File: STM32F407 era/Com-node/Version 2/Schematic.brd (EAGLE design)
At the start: 127 x 165.1 mm, 92 parts, among them IC2 lm2575, IC5 REG1117, Q2 12MHz, Q3 12MHz, U1 MAX13052ESA+, U2 SMS05, U3 MAX232AEWE+, X1 SDBMF, X5 679105700

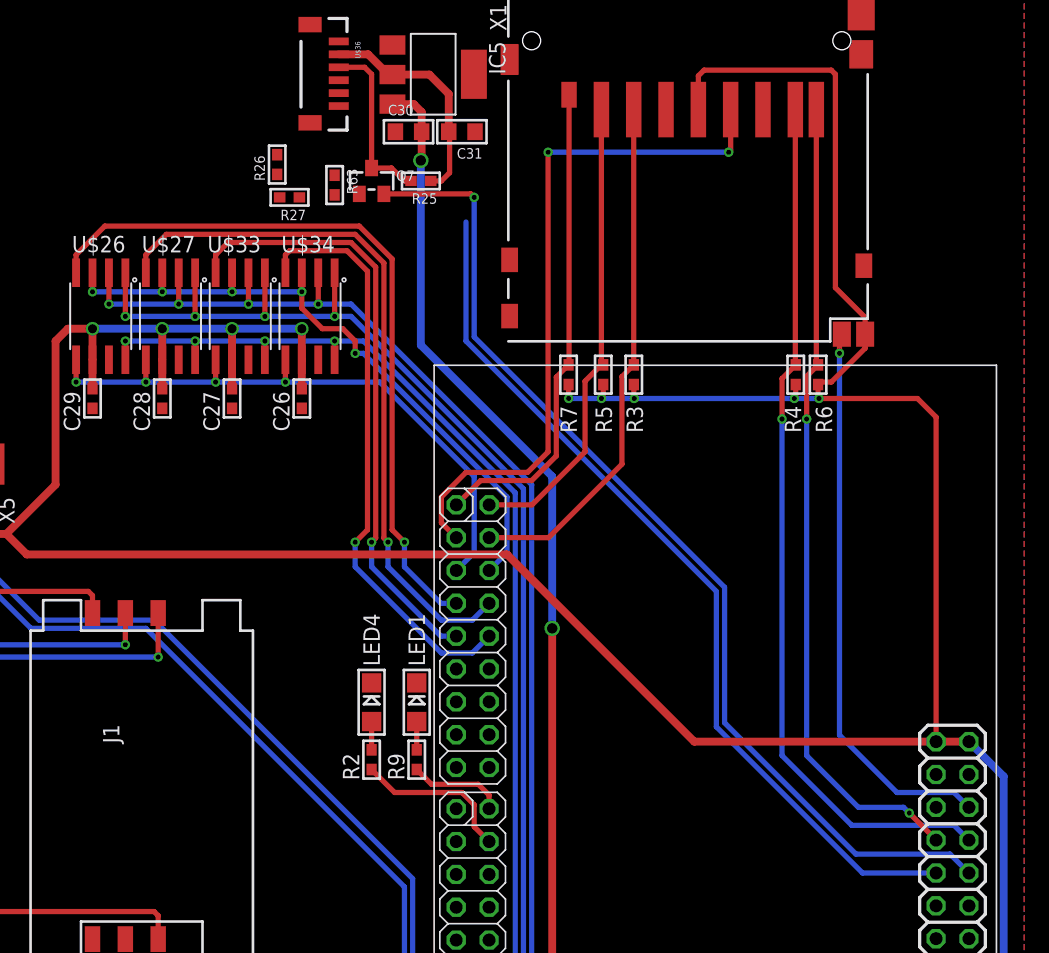
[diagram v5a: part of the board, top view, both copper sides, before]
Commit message: continued work on H-bridge
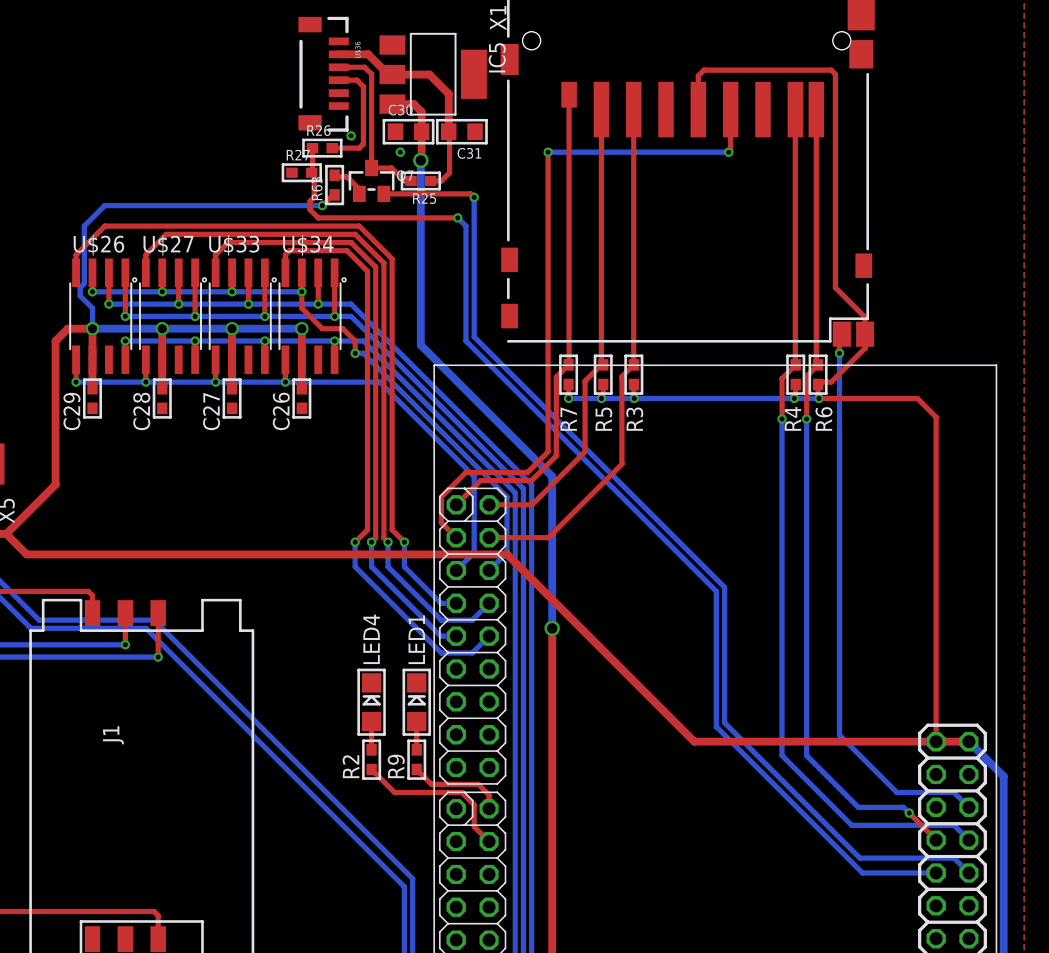
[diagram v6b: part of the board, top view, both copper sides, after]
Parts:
- moved R26 3.72 mm to (64.8, 140.3), turned to 0 degrees
- moved R27 2.13 mm to (63.2, 138.4), turned to 0 degrees
- turned R63 to 90 degrees
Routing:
- net 3.3V: track 573.3 -> 602.1 mm, vias 15 -> 16
- net GPS_RX: track 68.8 -> 86.0 mm, vias 0 -> 1
- net RXD1: track 0.00 -> 9.10 mm
- net N$58: track 0.00 -> 2.72 mm
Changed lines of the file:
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@@
 <element name="Q7" library="microbuilder" package="SOT23-WIDE" value="" x="68.58" y="137.795"/>
 <element name="R25" library="microbuilder" package="_0603" value="500" x="72.39" y="137.795" rot="R180"/>
-<element name="R63" library="microbuilder" package="_0603" value="500" x="65.7225" y="137.4775" rot="R270"/>
-<element name="R26" library="microbuilder" package="_0603" value="499" x="61.2775" y="139.065" rot="R90"/>
-<element name="R27" library="microbuilder" package="_0603" value="976" x="62.23" y="136.525" rot="R180"/>
+<element name="R63" library="microbuilder" package="_0603" value="500" x="65.7225" y="137.4775" rot="R90"/>
+<element name="R26" library="microbuilder" package="_0603" value="499" x="64.77" y="140.335"/>
+<element name="R27" library="microbuilder" package="_0603" value="976" x="63.1825" y="138.43"/>
 </elements>
 <signals>
@@
 <contactref element="C31" pad="1"/>
 <contactref element="R27" pad="1"/>
-<wire x1="70.4215" y1="141.605" x2="66.04" y2="144.59" width="0" layer="19" extent="1-1"/>
+<via x="70.8025" y="140.0175" extent="1-16" drill="0.381"/>
+<via x="66.9925" y="141.2875" extent="1-16" drill="0.381"/>
 </signal>
 <signal name="3.3V">
@@
 <wire x1="112.2045" y1="24.5745" x2="113.03" y2="24.5745" width="0.6096" layer="1"/>
 <contactref element="R63" pad="1"/>
-<wire x1="63.1825" y1="126.365" x2="65.7225" y2="138.2395" width="0" layer="19" extent="1-1"/>
+<wire x1="65.7225" y1="136.7155" x2="65.5955" y2="136.7155" width="0.4064" layer="1"/>
+<wire x1="65.5955" y1="136.7155" x2="64.77" y2="135.89" width="0.4064" layer="1"/>
+<via x="64.77" y="135.89" extent="1-16" drill="0.381"/>
+<wire x1="64.77" y1="135.89" x2="47.9425" y2="135.89" width="0.4064" layer="16"/>
+<wire x1="47.9425" y1="135.89" x2="46.355" y2="134.3025" width="0.4064" layer="16"/>
+<wire x1="46.355" y1="134.3025" x2="46.355" y2="129.8575" width="0.4064" layer="16"/>
+<wire x1="46.355" y1="129.8575" x2="46.0375" y2="129.54" width="0.4064" layer="16"/>
+<wire x1="46.0375" y1="129.54" x2="46.0375" y2="128.905" width="0.4064" layer="16"/>
+<wire x1="46.0375" y1="128.905" x2="46.99" y2="127.9525" width="0.4064" layer="16"/>
+<wire x1="46.99" y1="127.9525" x2="46.99" y2="126.365" width="0.4064" layer="16"/>
 </signal>
 <signal name="N$1">
@@
 <contactref element="U$36" pad="4"/>
 <contactref element="R26" pad="2"/>
-<wire x1="61.2775" y1="139.827" x2="66.04" y2="145.59" width="0" layer="19" extent="1-1"/>
+<wire x1="66.04" y1="145.59" x2="67.4525" y2="145.59" width="0.4064" layer="1"/>
+<wire x1="67.4525" y1="145.59" x2="67.945" y2="145.0975" width="0.4064" layer="1"/>
+<wire x1="67.945" y1="145.0975" x2="67.945" y2="140.6525" width="0.4064" layer="1"/>
+<wire x1="67.945" y1="140.6525" x2="67.6275" y2="140.335" width="0.4064" layer="1"/>
+<wire x1="67.6275" y1="140.335" x2="65.532" y2="140.335" width="0.4064" layer="1"/>
 </signal>
 <signal name="GPS_RX">
@@
 <wire x1="95.25" y1="95.5675" x2="95.25" y2="106.045" width="0.4064" layer="16"/>
 <wire x1="95.25" y1="106.045" x2="75.8825" y2="125.4125" width="0.4064" layer="16"/>
-<wire x1="75.8825" y1="125.4125" x2="75.8825" y2="134.62" width="0.4064" layer="16"/>
-<wire x1="61.468" y1="136.525" x2="61.2775" y2="138.303" width="0" layer="19" extent="1-1"/>
-<wire x1="75.8825" y1="134.62" x2="61.468" y2="136.525" width="0" layer="19" extent="1-16"/>
+<wire x1="75.8825" y1="125.4125" x2="75.8825" y2="134.3025" width="0.4064" layer="16"/>
+<wire x1="64.008" y1="140.335" x2="64.008" y2="138.4935" width="0.4064" layer="1"/>
+<wire x1="64.008" y1="138.4935" x2="63.9445" y2="138.43" width="0.4064" layer="1"/>
+<wire x1="63.8175" y1="135.5725" x2="64.4525" y2="134.9375" width="0.4064" layer="1"/>
+<wire x1="64.4525" y1="134.9375" x2="75.2475" y2="134.9375" width="0.4064" layer="1"/>
+<via x="75.2475" y="134.9375" extent="1-16" drill="0.381"/>
+<wire x1="75.2475" y1="134.9375" x2="75.8825" y2="134.3025" width="0.4064" layer="16"/>
+<wire x1="63.8175" y1="135.5725" x2="63.8175" y2="136.2075" width="0.4064" layer="1"/>
+<wire x1="63.8175" y1="136.2075" x2="64.135" y2="136.525" width="0.4064" layer="1"/>
+<wire x1="64.135" y1="136.525" x2="64.135" y2="138.2395" width="0.4064" layer="1"/>
+<wire x1="64.135" y1="138.2395" x2="63.9445" y2="138.43" width="0.4064" layer="1"/>
 </signal>
 <signal name="GPS_TX">
 <contactref element="U$1" pad="P$35"/>
 <contactref element="Q7" pad="2"/>
-<wire x1="114.78745" y1="84.26215" x2="113.3246" y2="85.725" width="0.4064" layer="16"/>
-<wire x1="113.3246" y1="85.725" x2="106.045" y2="85.725" width="0.4064" layer="16"/>
-<wire x1="106.045" y1="85.725" x2="95.885" y2="95.885" width="0.4064" layer="16"/>
+<wire x1="114.78745" y1="84.26215" x2="113.6421" y2="85.4075" width="0.4064" layer="16"/>
+<wire x1="113.6421" y1="85.4075" x2="106.3625" y2="85.4075" width="0.4064" layer="16"/>
+<wire x1="106.3625" y1="85.4075" x2="95.885" y2="95.885" width="0.4064" layer="16"/>
 <wire x1="95.885" y1="95.885" x2="95.885" y2="106.3625" width="0.4064" layer="16"/>
 <wire x1="95.885" y1="106.3625" x2="76.5175" y2="125.73" width="0.4064" layer="16"/>
@@
 <contactref element="Q7" pad="1"/>
 <contactref element="R63" pad="2"/>
-<wire x1="65.7225" y1="136.7155" x2="67.63" y2="136.795" width="0" layer="19" extent="1-1"/>
+<wire x1="67.63" y1="136.795" x2="67.63" y2="137.1575" width="0.4064" layer="1"/>
+<wire x1="67.63" y1="137.1575" x2="66.675" y2="138.1125" width="0.4064" layer="1"/>
+<wire x1="66.675" y1="138.1125" x2="65.8495" y2="138.1125" width="0.4064" layer="1"/>
+<wire x1="65.8495" y1="138.1125" x2="65.7225" y2="138.2395" width="0.4064" layer="1"/>
 </signal>
 </signals>
+<errors>
+</errors>
 </board>
 </drawing>

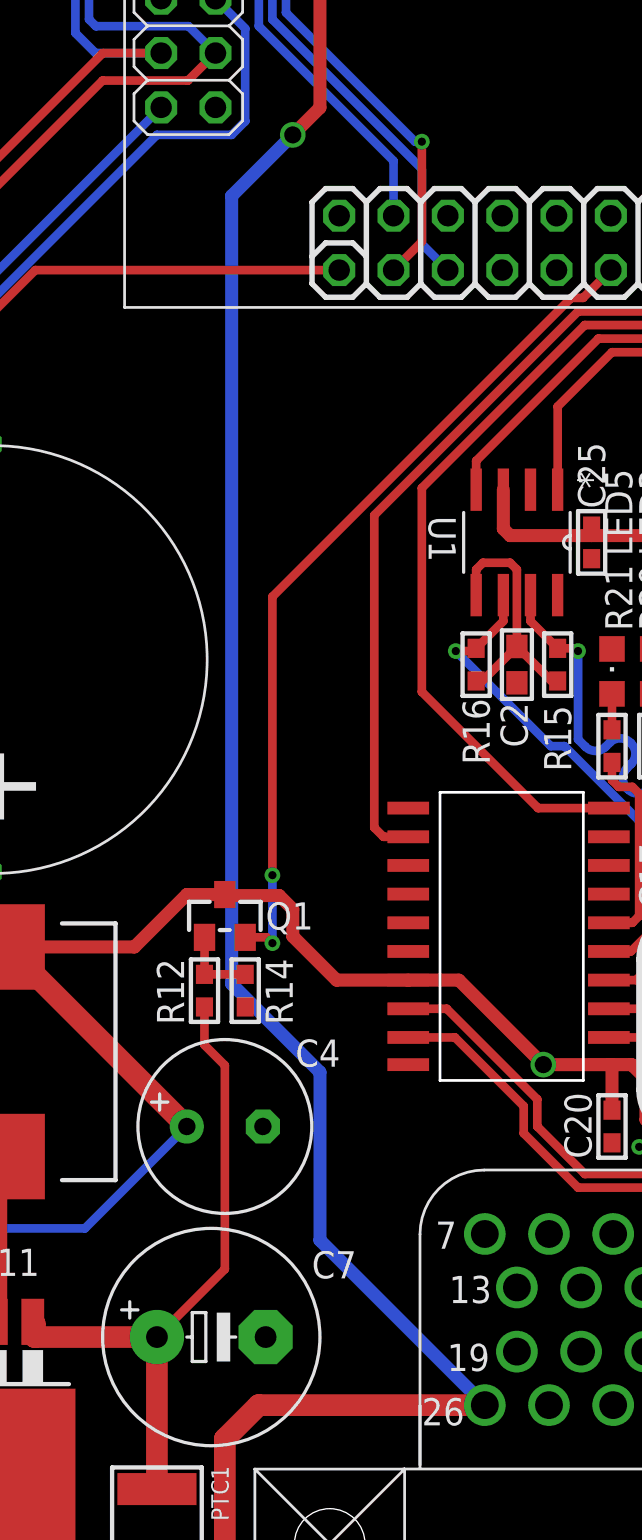
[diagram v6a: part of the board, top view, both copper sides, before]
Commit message: fixed 12V error with PTC fuse. Started work on new Dev Board
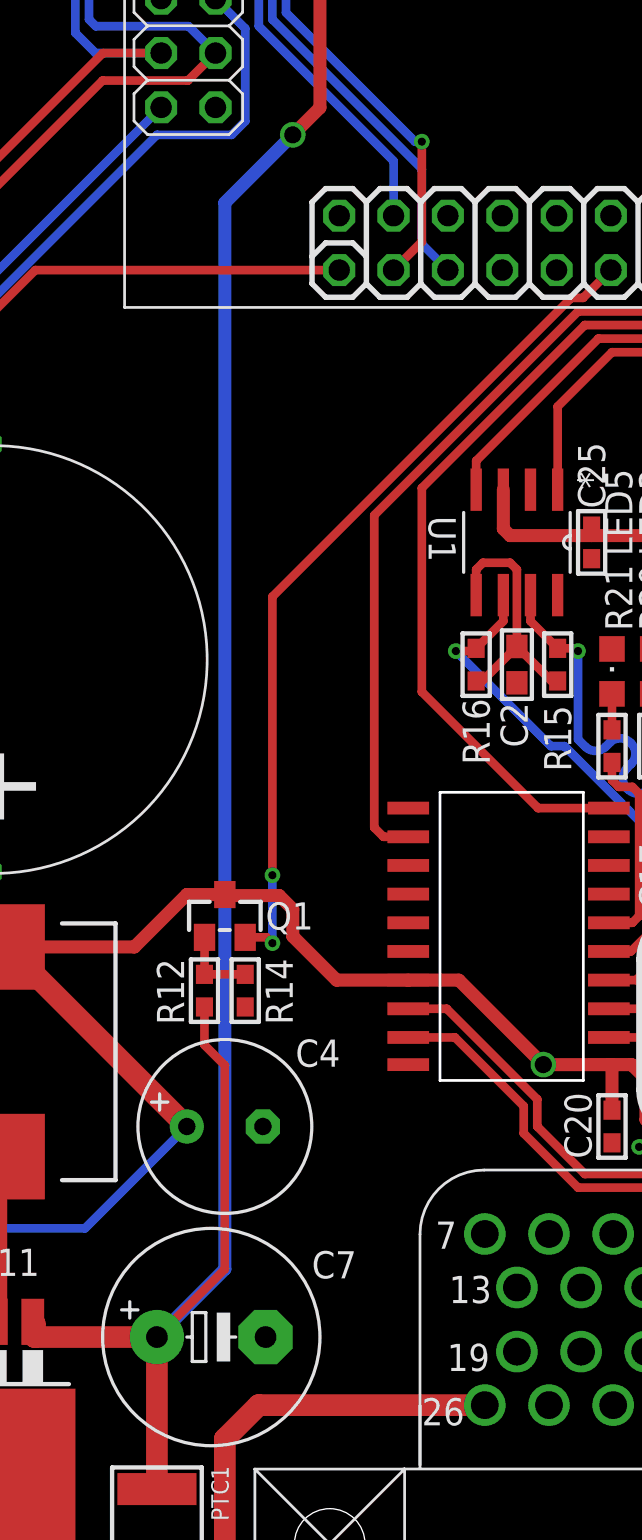
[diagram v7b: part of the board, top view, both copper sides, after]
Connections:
- removed net N$57: C7.+, IC2.1, PTC1.P$1, R12.1
- new net VCC: PTC1.P$2, U$18.26
- net 12V: now also C7.+, IC2.1, PTC1.P$1, R12.1; no longer PTC1.P$2, U$18.26
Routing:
- net N$57: track 30.7 -> 0.00 mm
- net VCC: track 0.00 -> 22.0 mm
- net 12V: track 167.7 -> 169.8 mm
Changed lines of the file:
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@@
 </signal>
 <signal name="12V">
-<contactref element="U$18" pad="26"/>
-<contactref element="PTC1" pad="P$2"/>
-<wire x1="90.2575" y1="10.7875" x2="79.685" y2="10.7875" width="1.016" layer="1"/>
-<wire x1="79.685" y1="10.7875" x2="78.105" y2="9.2075" width="1.016" layer="1"/>
-<wire x1="78.105" y1="9.2075" x2="78.105" y2="3.4925" width="1.016" layer="1"/>
-<wire x1="78.105" y1="3.4925" x2="77.275" y2="2.6625" width="1.016" layer="1"/>
-<wire x1="77.275" y1="2.6625" x2="74.93" y2="2.6625" width="1.016" layer="1"/>
 <contactref element="IC5" pad="3"/>
 <contactref element="C30" pad="2"/>
@@
 <wire x1="71.8439" y1="143.7386" x2="72.4535" y2="143.129" width="0.6096" layer="1"/>
 <wire x1="72.4535" y1="143.129" x2="72.4535" y2="141.605" width="0.6096" layer="1"/>
-<wire x1="90.2575" y1="10.7875" x2="82.55" y2="18.495" width="0.6096" layer="16"/>
-<wire x1="82.55" y1="18.495" x2="82.55" y2="26.3525" width="0.6096" layer="16"/>
-<wire x1="82.55" y1="26.3525" x2="78.4225" y2="30.48" width="0.6096" layer="16"/>
-<wire x1="78.4225" y1="30.48" x2="78.4225" y2="67.31" width="0.6096" layer="16"/>
-<wire x1="78.4225" y1="67.31" x2="81.28" y2="70.1675" width="0.6096" layer="16"/>
+<wire x1="78.105" y1="66.9925" x2="81.28" y2="70.1675" width="0.6096" layer="16"/>
 <via x="81.28" y="70.1675" extent="1-16" drill="0.8"/>
 <wire x1="81.28" y1="70.1675" x2="82.55" y2="71.4375" width="0.6096" layer="1"/>
@@
 <wire x1="72.39" y1="139.3825" x2="72.4535" y2="139.446" width="0.6096" layer="1"/>
 <wire x1="72.4535" y1="139.446" x2="72.4535" y2="141.605" width="0.6096" layer="1"/>
+<contactref element="IC2" pad="1"/>
+<contactref element="C7" pad="+"/>
+<contactref element="R12" pad="1"/>
+<contactref element="PTC1" pad="P$1"/>
+<wire x1="74.93" y1="13.97" x2="69.215" y2="13.97" width="1.016" layer="1"/>
+<wire x1="69.215" y1="13.97" x2="69.215" y2="14.5923" width="1.016" layer="1"/>
+<wire x1="69.215" y1="14.5923" x2="69.1261" y2="14.6812" width="1.016" layer="1"/>
+<wire x1="74.93" y1="13.97" x2="78.105" y2="17.145" width="0.4064" layer="1"/>
+<wire x1="78.105" y1="17.145" x2="78.105" y2="26.67" width="0.4064" layer="1"/>
+<wire x1="78.105" y1="26.67" x2="77.1525" y2="27.6225" width="0.4064" layer="1"/>
+<wire x1="77.1525" y1="27.6225" x2="77.1525" y2="29.4005" width="0.4064" layer="1"/>
+<wire x1="74.93" y1="13.97" x2="74.93" y2="6.8625" width="1.016" layer="1"/>
+<wire x1="78.105" y1="66.9925" x2="78.105" y2="17.145" width="0.6096" layer="16"/>
+<wire x1="78.105" y1="17.145" x2="74.93" y2="13.97" width="0.6096" layer="16"/>
 </signal>
 <signal name="COMRX">
@@
 <contactref element="LED1" pad="A"/>
 <wire x1="72.0725" y1="93.7895" x2="72.0725" y2="95.9765" width="0.4064" layer="1"/>
-</signal>
-<signal name="N$57">
-<contactref element="IC2" pad="1"/>
-<contactref element="C7" pad="+"/>
-<contactref element="R12" pad="1"/>
-<wire x1="74.93" y1="13.97" x2="69.215" y2="13.97" width="1.016" layer="1"/>
-<wire x1="69.215" y1="13.97" x2="69.215" y2="14.5923" width="1.016" layer="1"/>
-<wire x1="69.215" y1="14.5923" x2="69.1261" y2="14.6812" width="1.016" layer="1"/>
-<wire x1="74.93" y1="13.97" x2="78.105" y2="17.145" width="0.4064" layer="1"/>
-<wire x1="78.105" y1="17.145" x2="78.105" y2="26.67" width="0.4064" layer="1"/>
-<wire x1="78.105" y1="26.67" x2="77.1525" y2="27.6225" width="0.4064" layer="1"/>
-<wire x1="77.1525" y1="27.6225" x2="77.1525" y2="29.4005" width="0.4064" layer="1"/>
-<contactref element="PTC1" pad="P$1"/>
-<wire x1="74.93" y1="13.97" x2="74.93" y2="6.8625" width="1.016" layer="1"/>
 </signal>
 <signal name="SCK">
@@
 <wire x1="65.8495" y1="138.1125" x2="65.7225" y2="138.2395" width="0.4064" layer="1"/>
 </signal>
+<signal name="VCC">
+<contactref element="PTC1" pad="P$2"/>
+<contactref element="U$18" pad="26"/>
+<wire x1="90.2575" y1="10.7875" x2="79.685" y2="10.7875" width="1.016" layer="1"/>
+<wire x1="79.685" y1="10.7875" x2="78.105" y2="9.2075" width="1.016" layer="1"/>
+<wire x1="78.105" y1="9.2075" x2="78.105" y2="3.4925" width="1.016" layer="1"/>
+<wire x1="78.105" y1="3.4925" x2="77.275" y2="2.6625" width="1.016" layer="1"/>
+<wire x1="77.275" y1="2.6625" x2="74.93" y2="2.6625" width="1.016" layer="1"/>
+</signal>
 </signals>

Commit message: created Gerbers
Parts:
- U$24, U$29: value MCP2200SOIC -> MCP2200; device mcp2200:MCP2200 -> mcp2200:SO20L
- moved U$24 7.65 mm to (90.5, 32.4)
- moved U$29 7.18 mm to (108.3, 32.4)
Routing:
- net N$44: track 8.99 -> 13.0 mm, vias 0 -> 2
- net 3.3V: track 602.1 -> 598.6 mm, vias 16 -> 17
- net COMTX: track 44.9 -> 46.5 mm
- net COMD+: track 21.4 -> 22.6 mm
- net COMD-: track 20.7 -> 21.9 mm
- net ECUTX: track 11.7 -> 12.5 mm
- net N$29: track 9.62 -> 10.3 mm
- net N$36: track 10.3 -> 10.9 mm
- net N$43: track 9.76 -> 10.4 mm
- net ECURX: track 2.93 -> 3.53 mm
- net N$27: track 8.32 -> 8.90 mm
- net ECUD+: track 14.2 -> 14.8 mm
- net ECUD-: track 13.4 -> 14.0 mm
- net N$26: track 8.46 -> 8.99 mm
